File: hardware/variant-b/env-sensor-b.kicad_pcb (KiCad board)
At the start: 4 copper layers, 30 x 51 mm, 64 parts, among them J1 USB-C 16P, J2 Molex PicoBlade 3P, Q1 2N7002, SW1 SW_PROV, U1 ESP32-C6-MINI-1-N4, U2 SHT45-AD1F, U3 TPS62840DLC, U4 BQ24074RGTR, U5 USBLC6-2SC6

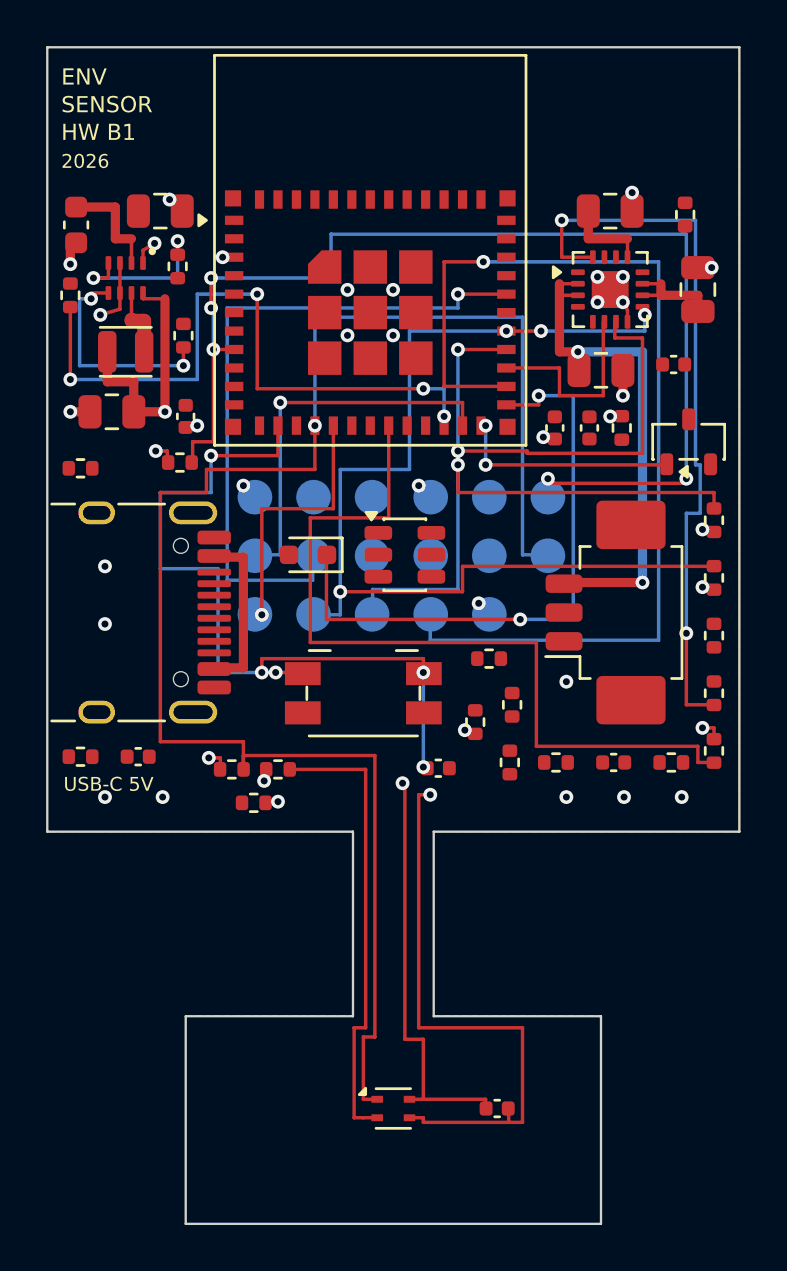
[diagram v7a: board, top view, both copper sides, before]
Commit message: build(boardgen): regenerate paste-safe routing for both variants
Regenerate from the ordinary-via paste separation correction. Fresh KiCad reports show zero errors, warnings and parity differences; record the exact incomplete development counts of A42/B34. Fabrication still requires complete routing and accepted qualification evidence.
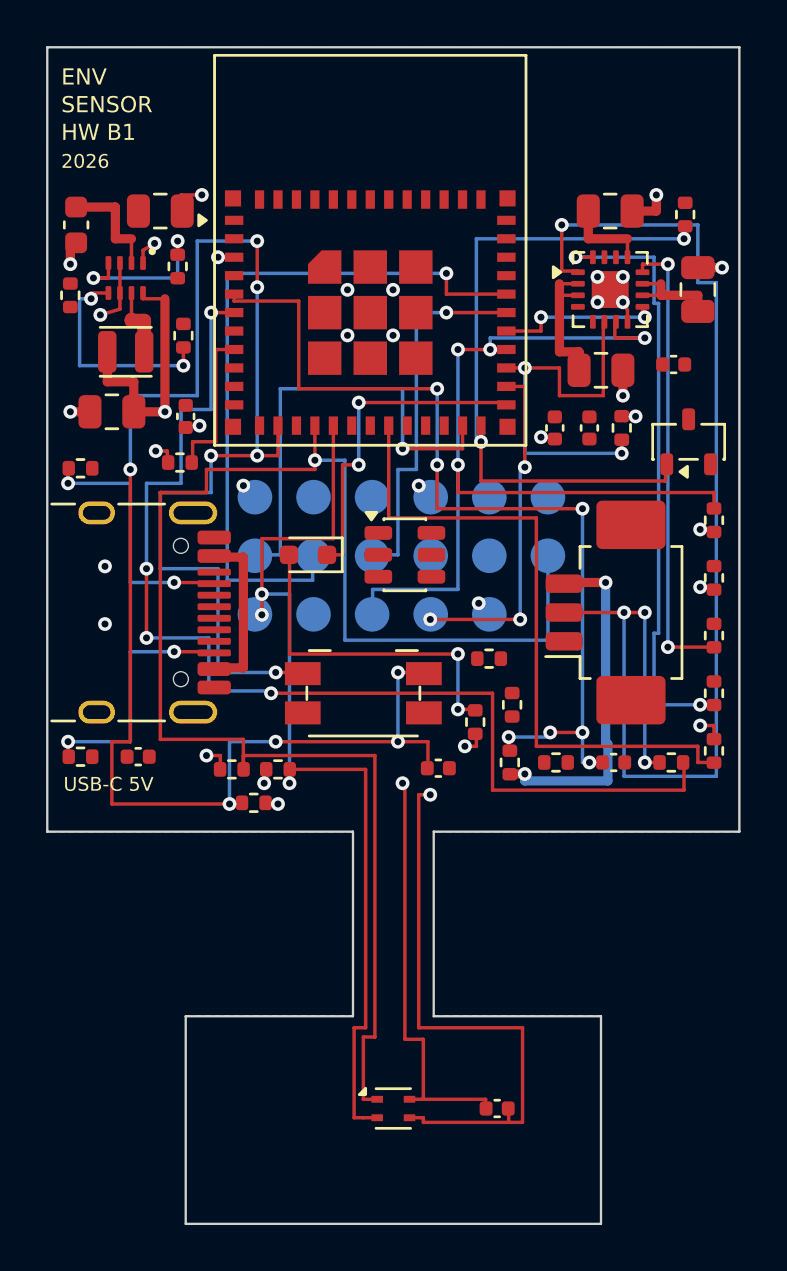
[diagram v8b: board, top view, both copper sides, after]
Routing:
- net PACK_TS: track 0.00 -> 55.1 mm, vias 0 -> 4
- net BTN_PROV: track 34.3 -> 84.1 mm, vias 5 -> 10
- net PACK_TS_SENSE: track 0.00 -> 49.0 mm, vias 0 -> 4
- net EN: track 50.2 -> 6.70 mm, vias 5 -> 0
- net VBAT_SENSE: track 0.00 -> 40.3 mm, vias 0 -> 7
- net CHG_N: track 45.2 -> 7.20 mm, vias 4 -> 2
- net TEST_MODE: track 44.8 -> 15.0 mm, vias 1 -> 3
- net BOOT_MODE_H: track 28.7 -> 0.00 mm, vias 4 -> 0
- net CHARGE_ENABLE: track 9.50 -> 29.6 mm
- net ILIM: track 0.00 -> 20.1 mm, vias 0 -> 2
- net UART_RX: track 0.00 -> 16.3 mm, vias 0 -> 1
- net LED_A: track 0.00 -> 14.8 mm, vias 0 -> 2
- net LED_N: track 26.5 -> 14.5 mm
- net CC1: track 0.00 -> 11.3 mm, vias 0 -> 2
- net CC2: track 0.00 -> 10.9 mm, vias 0 -> 2
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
